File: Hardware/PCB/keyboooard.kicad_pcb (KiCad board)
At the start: 2 copper layers, 318 x 134 mm, 155 parts, among them J1 OLED_128x32, SW1 SW_Push_45deg, SW10 SW_Push_45deg, SW11 SW_Push_45deg, SW12 SW_Push_45deg, SW13 SW_Push_45deg, SW14 SW_Push_45deg, SW15 SW_Push_45deg, SW16 SW_Push_45deg, SW17 SW_Push_45deg, SW18 SW_Push_45deg, SW19 SW_Push_45deg, SW2 SW_Push_45deg, SW20 SW_Push_45deg, SW21 SW_Push_45deg, SW22 SW_Push_45deg, SW23 SW_Push_45deg, SW24 SW_Push_45deg, SW25 SW_Push_45deg, SW26 SW_Push_45deg, SW27 SW_Push_45deg, SW28 SW_Push_45deg, SW29 SW_Push_45deg, SW3 SW_Push_45deg, SW30 SW_Push_45deg, SW31 SW_Push_45deg, SW32 SW_Push_45deg, SW33 SW_Push_45deg, SW34 SW_Push_45deg, SW35 SW_Push_45deg, SW36 SW_Push_45deg, SW37 SW_Push_45deg, SW38 SW_Push_45deg, SW39 SW_Push_45deg, SW4 SW_Push_45deg, SW40 SW_Push_45deg, SW41 SW_Push_45deg, SW42 SW_Push_45deg, SW43 SW_Push_45deg, SW44 SW_Push_45deg, SW45 SW_Push_45deg, SW46 SW_Push_45deg, SW47 SW_Push_45deg, SW48 SW_Push_45deg, SW49 SW_Push_45deg, SW5 SW_Push_45deg, SW50 SW_Push_45deg, SW51 SW_Push_45deg, SW52 SW_Push_45deg, SW53 SW_Push_45deg, SW54 SW_Push_45deg, SW55 SW_Push_45deg, SW56 SW_Push_45deg, SW57 SW_Push_45deg, SW58 SW_Push_45deg, SW59 SW_Push_45deg, SW6 SW_Push_45deg, SW60 SW_Push_45deg, SW61 SW_Push_45deg, SW62 SW_Push_45deg, SW63 SW_Push_45deg, SW64 SW_Push_45deg, SW65 SW_Push_45deg, SW66 SW_Push_45deg, SW67 SW_Push_45deg, SW68 SW_Push_45deg, SW7 SW_Push_45deg, SW8 SW_Push_45deg, SW9 SW_Push_45deg, U1 RP2040_Pro_Micro

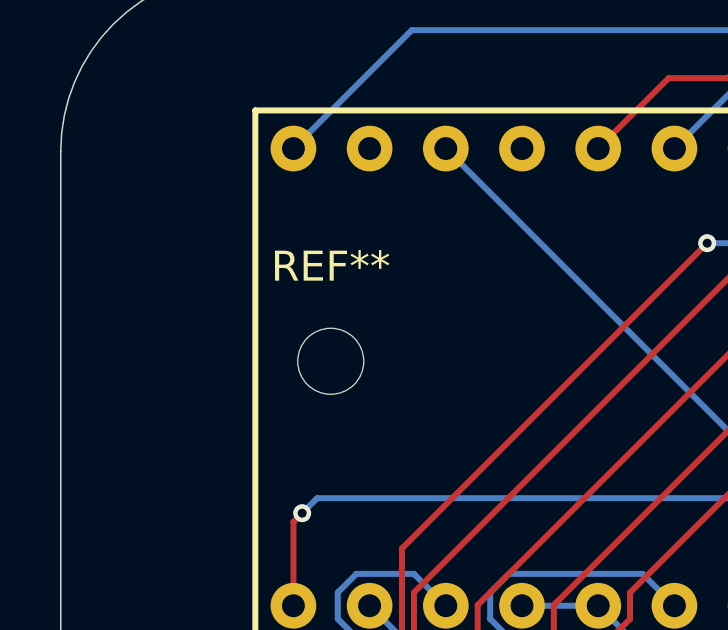
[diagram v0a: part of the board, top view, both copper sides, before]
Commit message: update pcb mounting hole 11
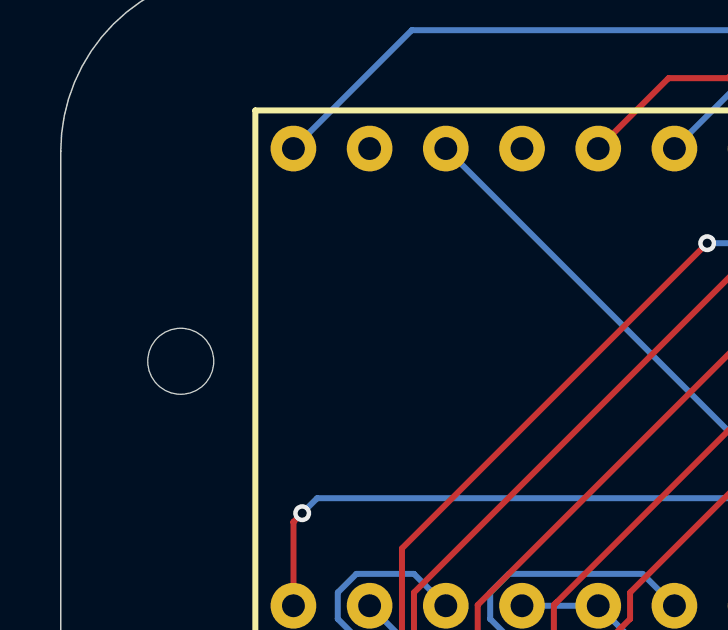
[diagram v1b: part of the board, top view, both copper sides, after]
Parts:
- moved REF** 5.00 mm to (60.5, 75.8)
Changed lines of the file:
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@@
 			(drillshape 0)
 			(scaleselection 1)
-			(outputdirectory "gerbers/")
+			(outputdirectory "gerbers/temp")
 		)
 	)
@@
 	(footprint "MountingHole:MountingHole_2.2mm_M2"
 		(layer "F.Cu")
-		(at 65.520195 75.819883)
+		(at 60.520195 75.819883)
 		(descr "Mounting Hole 2.2mm, M2, no annular, generated by kicad-footprint-generator mountinghole.py")
 		(tags "mountinghole M2")
@@
 			(at 0 -3.15 0)
 			(layer "F.SilkS")
+			(hide yes)
 			(effects
 				(font

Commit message: final update: cad, zine page, bom
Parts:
- added REF**: MountingHole_2.2mm_M2, MountingHole:MountingHole_2.2mm_M2, F.Cu at (156.5, 73.8)
- moved REF** 47.0 mm to (107.5, 73.8)
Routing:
- net GND: track 307.5 -> 24.1 mm, vias 0 -> 11
- net ROW4: track 631.8 -> 800.8 mm
- net ROW2: track 402.0 -> 429.4 mm
- net COL2: track 144.8 -> 131.1 mm, vias 2 -> 1
- added copper zone on B.Cu, net GND
- added copper zone on F.Cu, net GND
